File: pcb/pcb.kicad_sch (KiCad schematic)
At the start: 39 parts, among them J3 BAT, U1 xiao-ble

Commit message: rename to Charma
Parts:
- DL1, DL10, DL11, DL12, DL13, DL14, DL15, DL17, DL18, DL19, DL2, DL3, DL4, DL5, DL6, DL7, DL8, DL9: footprint karmalib:Diode_SOD123 -> charmalib:Diode_SOD123
- RSW1: footprint karmalib:SKHLLCA010 -> charmalib:SKHLLCA010
- SWL1, SWL10, SWL11, SWL12, SWL13, SWL14, SWL15, SWL17, SWL18, SWL19, SWL2, SWL3, SWL4, SWL5, SWL6, SWL7, SWL8, SWL9: footprint karmalib:Kailh_Socket_PG1350_Optional -> charmalib:Kailh_Socket_PG1350_Optional
- U1: footprint karmalib:XIAO_nRF52840_SMD_Cutout -> charmalib:XIAO_nRF52840_SMD_Cutout
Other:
- title: Karma Wireless Split Ergonomic Keyboard -> Charma Wireless Split Ergonomic Keyboard
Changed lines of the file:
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@@
 	(paper "User" 200 200)
 	(title_block
-		(title "Karma Wireless Split Ergonomic Keyboard")
+		(title "Charma Wireless Split Ergonomic Keyboard")
 		(date "2023-04-04")
 		(rev "0.32")
@@
 			)
 		)
-		(property "Footprint" "karmalib:Kailh_Socket_PG1350_Optional"
+		(property "Footprint" "charmalib:Kailh_Socket_PG1350_Optional"
 			(at 62.23 99.187 0)
 			(effects
@@
 			)
 		)
-		(property "Footprint" "karmalib:Kailh_Socket_PG1350_Optional"
+		(property "Footprint" "charmalib:Kailh_Socket_PG1350_Optional"
 			(at 72.898 69.215 0)
 			(effects
@@
 			)
 		)
-		(property "Footprint" "karmalib:Diode_SOD123"
+		(property "Footprint" "charmalib:Diode_SOD123"
 			(at 86.106 104.267 90)
 			(effects
@@
 			)
 		)
-		(property "Footprint" "karmalib:Diode_SOD123"
+		(property "Footprint" "charmalib:Diode_SOD123"
 			(at 43.434 74.295 90)
 			(effects
@@
 			)
 		)
-		(property "Footprint" "karmalib:Diode_SOD123"
+		(property "Footprint" "charmalib:Diode_SOD123"
 			(at 75.438 74.295 90)
 			(effects
@@
 			)
 		)
-		(property "Footprint" "karmalib:SKHLLCA010"
+		(property "Footprint" "charmalib:SKHLLCA010"
 			(at 148.0312 131.4704 0)
 			(effects
@@
 			)
 		)
-		(property "Footprint" "karmalib:Kailh_Socket_PG1350_Optional"
+		(property "Footprint" "charmalib:Kailh_Socket_PG1350_Optional"
 			(at 83.566 54.229 0)
 			(effects
@@
 			)
 		)
-		(property "Footprint" "karmalib:Kailh_Socket_PG1350_Optional"
+		(property "Footprint" "charmalib:Kailh_Socket_PG1350_Optional"
 			(at 51.562 69.215 0)
 			(effects
@@
 			)
 		)
-		(property "Footprint" "karmalib:Kailh_Socket_PG1350_Optional"
+		(property "Footprint" "charmalib:Kailh_Socket_PG1350_Optional"
 			(at 40.894 84.201 0)
 			(effects
@@
 			)
 		)
-		(property "Footprint" "karmalib:Diode_SOD123"
+		(property "Footprint" "charmalib:Diode_SOD123"
 			(at 86.106 89.281 90)
 			(effects
@@
 			)
 		)
-		(property "Footprint" "karmalib:Kailh_Socket_PG1350_Optional"
+		(property "Footprint" "charmalib:Kailh_Socket_PG1350_Optional"
 			(at 83.566 69.215 0)
 			(effects
@@
 			)
 		)
-		(property "Footprint" "karmalib:Kailh_Socket_PG1350_Optional"
+		(property "Footprint" "charmalib:Kailh_Socket_PG1350_Optional"
 			(at 62.23 54.229 0)
 			(effects
@@
 			)
 		)
-		(property "Footprint" "karmalib:Kailh_Socket_PG1350_Optional"
+		(property "Footprint" "charmalib:Kailh_Socket_PG1350_Optional"
 			(at 72.898 84.201 0)
 			(effects
@@
 			)
 		)
-		(property "Footprint" "karmalib:Diode_SOD123"
+		(property "Footprint" "charmalib:Diode_SOD123"
 			(at 43.434 89.281 90)
 			(effects
@@
 			)
 		)
-		(property "Footprint" "karmalib:Kailh_Socket_PG1350_Optional"
+		(property "Footprint" "charmalib:Kailh_Socket_PG1350_Optional"
 			(at 62.23 69.215 0)
 			(effects
@@
 			)
 		)
-		(property "Footprint" "karmalib:Kailh_Socket_PG1350_Optional"
+		(property "Footprint" "charmalib:Kailh_Socket_PG1350_Optional"
 			(at 62.23 84.201 0)
 			(effects
@@
 			)
 		)
-		(property "Footprint" "karmalib:Diode_SOD123"
+		(property "Footprint" "charmalib:Diode_SOD123"
 			(at 64.77 104.267 90)
 			(effects
@@
 			)
 		)
-		(property "Footprint" "karmalib:Diode_SOD123"
+		(property "Footprint" "charmalib:Diode_SOD123"
 			(at 64.77 74.295 90)
 			(effects
@@
 			)
 		)
-		(property "Footprint" "karmalib:Diode_SOD123"
+		(property "Footprint" "charmalib:Diode_SOD123"
 			(at 75.438 59.309 90)
 			(effects
@@
 			)
 		)
-		(property "Footprint" "karmalib:Kailh_Socket_PG1350_Optional"
+		(property "Footprint" "charmalib:Kailh_Socket_PG1350_Optional"
 			(at 83.566 99.187 0)
 			(effects
@@
 			)
 		)
-		(property "Footprint" "karmalib:Kailh_Socket_PG1350_Optional"
+		(property "Footprint" "charmalib:Kailh_Socket_PG1350_Optional"
 			(at 40.894 69.215 0)
 			(effects
@@
 			)
 		)
-		(property "Footprint" "karmalib:Kailh_Socket_PG1350_Optional"
+		(property "Footprint" "charmalib:Kailh_Socket_PG1350_Optional"
 			(at 51.562 84.201 0)
 			(effects
@@
 			)
 		)
-		(property "Footprint" "karmalib:Kailh_Socket_PG1350_Optional"
+		(property "Footprint" "charmalib:Kailh_Socket_PG1350_Optional"
 			(at 51.562 54.229 0)
 			(effects
@@
 			)
 		)
-		(property "Footprint" "karmalib:Kailh_Socket_PG1350_Optional"
+		(property "Footprint" "charmalib:Kailh_Socket_PG1350_Optional"
 			(at 40.894 54.229 0)
 			(effects
@@
 			)
 		)
-		(property "Footprint" "karmalib:Kailh_Socket_PG1350_Optional"
+		(property "Footprint" "charmalib:Kailh_Socket_PG1350_Optional"
 			(at 72.898 54.229 0)
 			(effects
@@
 			)
 		)
-		(property "Footprint" "karmalib:Diode_SOD123"
+		(property "Footprint" "charmalib:Diode_SOD123"
 			(at 54.102 59.309 90)
 			(effects
@@
 			)
 		)
-		(property "Footprint" "karmalib:Diode_SOD123"
+		(property "Footprint" "charmalib:Diode_SOD123"
 			(at 64.77 59.309 90)
 			(effects
@@
 			)
 		)
-		(property "Footprint" "karmalib:XIAO_nRF52840_SMD_Cutout"
+		(property "Footprint" "charmalib:XIAO_nRF52840_SMD_Cutout"
 			(at 134.6708 68.7578 0)
 			(effects
@@
 			)
 		)
-		(property "Footprint" "karmalib:Diode_SOD123"
+		(property "Footprint" "charmalib:Diode_SOD123"
 			(at 43.434 59.309 90)
 			(effects
@@
 			)
 		)
-		(property "Footprint" "karmalib:Diode_SOD123"
+		(property "Footprint" "charmalib:Diode_SOD123"
 			(at 54.102 89.281 90)
 			(effects
@@
 			)
 		)
-		(property "Footprint" "karmalib:Kailh_Socket_PG1350_Optional"
+		(property "Footprint" "charmalib:Kailh_Socket_PG1350_Optional"
 			(at 72.898 99.187 0)
 			(effects
@@
 			)
 		)
-		(property "Footprint" "karmalib:Diode_SOD123"
+		(property "Footprint" "charmalib:Diode_SOD123"
 			(at 75.438 104.267 90)
 			(effects
@@
 			)
 		)
-		(property "Footprint" "karmalib:Diode_SOD123"
+		(property "Footprint" "charmalib:Diode_SOD123"
 			(at 54.102 74.295 90)
 			(effects
@@
 			)
 		)
-		(property "Footprint" "karmalib:Diode_SOD123"
+		(property "Footprint" "charmalib:Diode_SOD123"
 			(at 75.438 89.281 90)
 			(effects
@@
 			)
 		)
-		(property "Footprint" "karmalib:Diode_SOD123"
+		(property "Footprint" "charmalib:Diode_SOD123"
 			(at 86.106 74.295 90)
 			(effects
@@
 			)
 		)
-		(property "Footprint" "karmalib:Diode_SOD123"
+		(property "Footprint" "charmalib:Diode_SOD123"
 			(at 86.106 59.309 90)
 			(effects
@@
 			)
 		)
-		(property "Footprint" "karmalib:Kailh_Socket_PG1350_Optional"
+		(property "Footprint" "charmalib:Kailh_Socket_PG1350_Optional"
 			(at 83.566 84.201 0)
 			(effects
@@
 			)
 		)
-		(property "Footprint" "karmalib:Diode_SOD123"
+		(property "Footprint" "charmalib:Diode_SOD123"
 			(at 64.77 89.281 90)
 			(effects

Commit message: Parameterise
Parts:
- added DR19, DR20, DR21, DR22, DR23, DR24, DR25, DR26, DR27, DR28, DR29, DR30, DR31, DR32, DR33, DR34, DR35, DR36: D_Small, charmalib:Diode_SOD123, symbol Device:D_Small
- added J2: BAT, Connector_PinHeader_2.54mm:PinHeader_1x02_P2.54mm_Vertical, symbol Connector_Generic:Conn_01x02
- added RSW2: SW_Push, Button_Switch_SMD:SW_Push_1P1T-MP_NO_Horizontal_Alps_SKRTLAE010, symbol Switch:SW_Push
- added SWR1, SWR19, SWR2, SWR20, SWR21, SWR22, SWR23, SWR24, SWR25, SWR26, SWR27, SWR28, SWR29, SWR3, SWR4, SWR5, SWR6, SWR7: SW_Push_45deg, charmalib:Kailh_Socket_PG1350_Optional, symbol Switch:SW_Push_45deg
- added U2: xiao-ble, charmalib:XIAO_nRF52840_SMD_Cutout, symbol mcu:xiao-ble
- RSW1: footprint charmalib:SKHLLCA010 -> Button_Switch_SMD:SW_Push_1P1T-MP_NO_Horizontal_Alps_SKRTLAE010
- renumbered DL17 to DL16, DL18 to DL17, DL19 to DL18, J3 to J1, SWL17 to SWL16, SWL18 to SWL17, SWL19 to SWL18
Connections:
- new net: DR21.2 (A), SWR3.2
- new net: DR30.2 (A), SWR23.2
- new net: DR25.2 (A), SWR7.2
- new net: DR19.2 (A), SWR1.2
- new net: DR35.2 (A), SWR28.2
- new net: DR24.2 (A), SWR6.2
- new net: DR36.2 (A), SWR29.2
- new net: DR20.2 (A), SWR2.2
- new net: DR22.2 (A), SWR4.2
- new net: DR27.2 (A), SWR20.2
- new net: DR31.2 (A), SWR24.2
- new net: DR33.2 (A), SWR26.2
- new net: DR28.2 (A), SWR21.2
- new net: DR23.2 (A), SWR5.2
- new net: DR26.2 (A), SWR19.2
- new net: DR29.2 (A), SWR22.2
- new net: DR34.2 (A), SWR27.2
- new net: DR32.2 (A), SWR25.2
- new net COL0_R: SWR1.1, SWR22.1, SWR6.1, U2.5 (A8_SDA/0.04_H)
- new net COL1_R: SWR2.1, SWR23.1, SWR7.1, U2.6 (A9_SCL/0.05_H)
- new net COL2_R: SWR19.1, SWR24.1, SWR27.1, SWR3.1, U2.11 (A6_MOSI/1.15)
- new net COL3_R: SWR20.1, SWR25.1, SWR28.1, SWR4.1, U2.10 (A5_MISO/1.14)
- new net COL4_R: SWR21.1, SWR26.1, SWR29.1, SWR5.1, U2.9 (A7_SCK/1.13)
- new net GND_R: J2.1 (Pin_1), RSW2.2, U2.13 (GND), U2.18 (GND), U2.20 (GND)
- new net RESET_R: RSW2.1, U2.17 (RESET)
- new net ROW0_R: DR19.1 (K), DR20.1 (K), DR21.1 (K), DR22.1 (K), DR23.1 (K), U2.4 (A11/0.29)
- new net ROW1_R: DR24.1 (K), DR25.1 (K), DR26.1 (K), DR27.1 (K), DR28.1 (K), U2.3 (A10/0.28)
- new net ROW2_R: DR29.1 (K), DR30.1 (K), DR31.1 (K), DR32.1 (K), DR33.1 (K), U2.2 (A4/0.03_H)
- new net ROW3_R: DR34.1 (K), DR35.1 (K), DR36.1 (K), U2.1 (A2/0.02_H)
- new net VBAT_R: J2.2 (Pin_2), U2.19 (BAT)
- no-connect marks 8 -> 16

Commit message: Update refs
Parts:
- renumbered J1 to BATL1, J2 to BATR1, DR19 to DR1, DR28 to DR10, DR29 to DR11, DR30 to DR12, DR31 to DR13, DR32 to DR14, DR33 to DR15, DR34 to DR16, DR35 to DR17, DR36 to DR18, DR20 to DR2, DR21 to DR3, DR22 to DR4, DR23 to DR5, DR24 to DR6, DR25 to DR7, DR26 to DR8, DR27 to DR9, U1 to MCUL1, U2 to MCUR2, RSW1 to RSWL1, RSW2 to RSWR1, SWR21 to SWR10, SWR22 to SWR11, SWR23 to SWR12, SWR24 to SWR13, SWR25 to SWR14, SWR26 to SWR15, SWR27 to SWR16, SWR28 to SWR17, SWR29 to SWR18, SWR19 to SWR8, SWR20 to SWR9

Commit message: Use SKQB for reset
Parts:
- RSWL1, RSWR1: footprint Button_Switch_SMD:SW_Push_1P1T-MP_NO_Horizontal_Alps_SKRTLAE010 -> Button_Switch_SMD:SW_SPST_SKQG_WithStem
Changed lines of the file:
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@@
 			)
 		)
-		(property "Footprint" "Button_Switch_SMD:SW_Push_1P1T-MP_NO_Horizontal_Alps_SKRTLAE010"
+		(property "Footprint" "Button_Switch_SMD:SW_SPST_SKQG_WithStem"
 			(at 344.3732 131.8514 0)
 			(effects
@@
 			)
 		)
-		(property "Footprint" "Button_Switch_SMD:SW_Push_1P1T-MP_NO_Horizontal_Alps_SKRTLAE010"
+		(property "Footprint" "Button_Switch_SMD:SW_SPST_SKQG_WithStem"
 			(at 148.0312 131.4704 0)
 			(effects

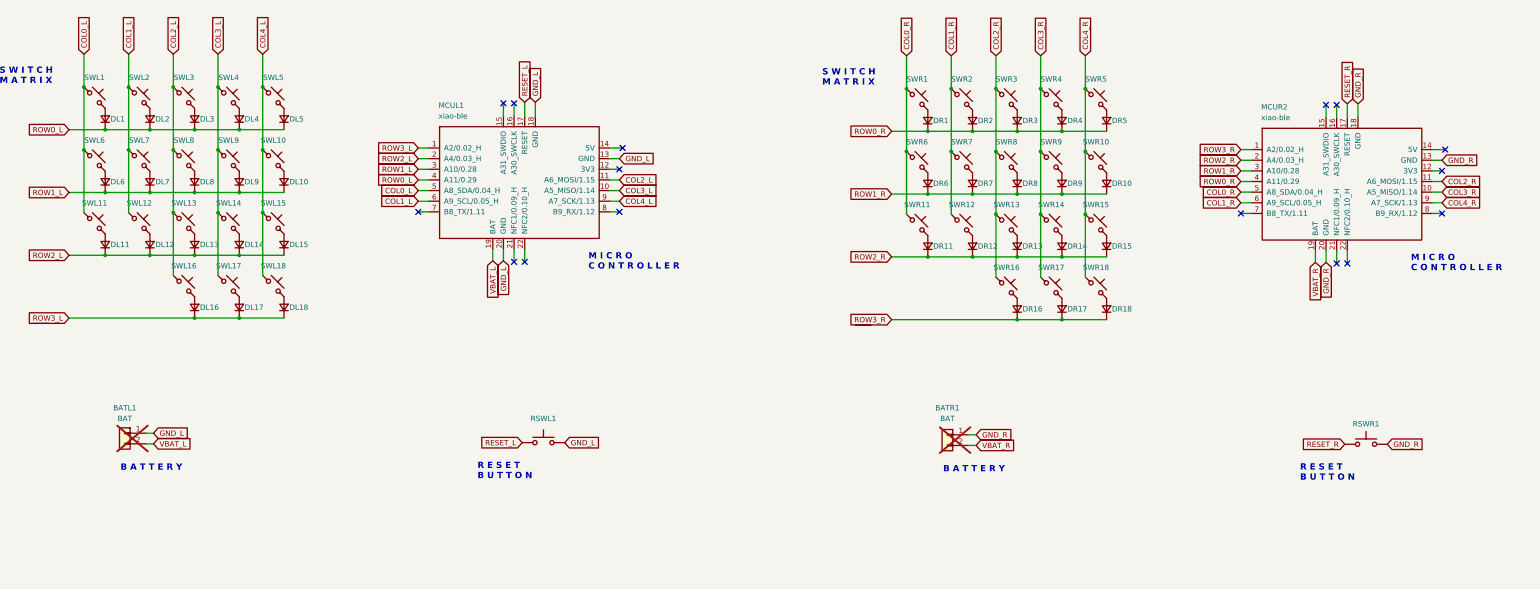
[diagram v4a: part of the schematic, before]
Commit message: Use socketed Xiao
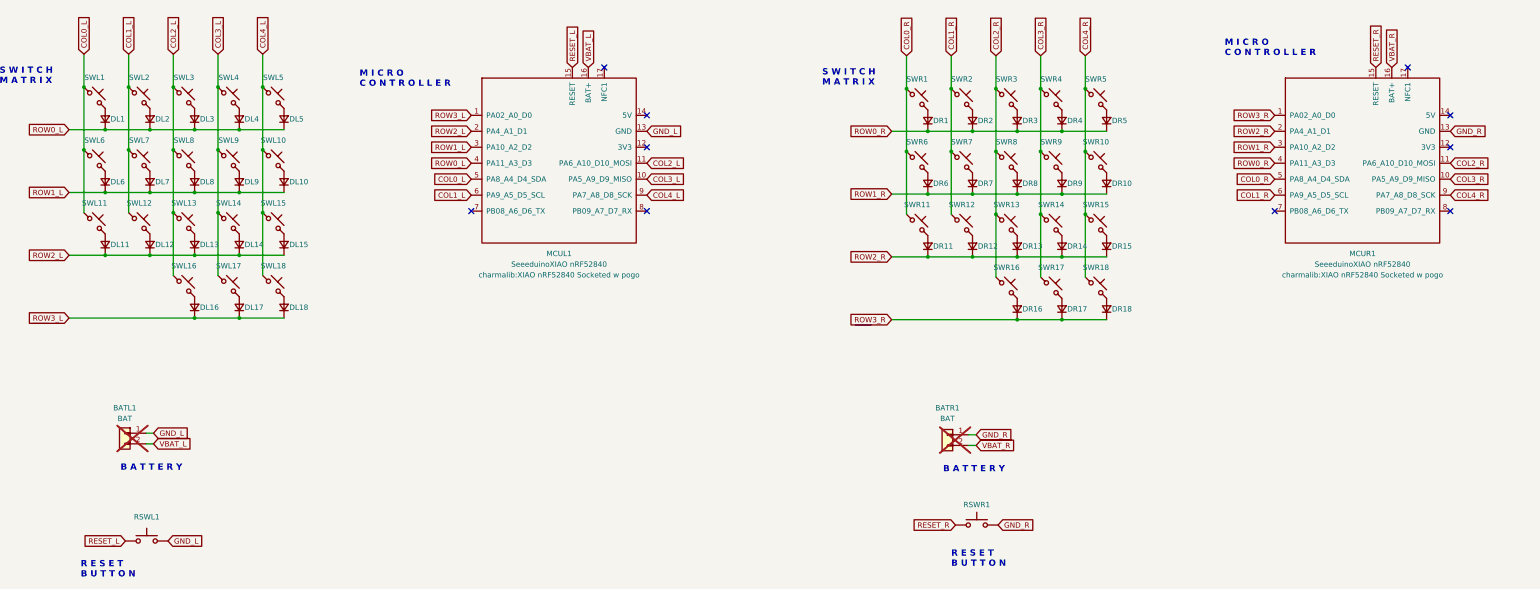
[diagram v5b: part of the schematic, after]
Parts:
- removed MCUL1, MCUR2: xiao-ble, charmalib:XIAO_nRF52840_SMD_Cutout, symbol mcu:xiao-ble
- added MCUL1, MCUR1: SeeeduinoXIAO nRF52840, charmalib:XIAO nRF52840 Socketed w pogo, symbol Xiao:Xiao nRF52840
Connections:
- net COL0_L: now also MCUL1.5 (PA8_A4_D4_SDA)
- net COL0_R: now also MCUR1.5 (PA8_A4_D4_SDA)
- net COL1_L: now also MCUL1.6 (PA9_A5_D5_SCL)
- net COL1_R: now also MCUR1.6 (PA9_A5_D5_SCL)
- net COL2_L: now also MCUL1.11 (PA6_A10_D10_MOSI)
- net COL2_R: now also MCUR1.11 (PA6_A10_D10_MOSI)
- net COL3_L: now also MCUL1.10 (PA5_A9_D9_MISO)
- net COL3_R: now also MCUR1.10 (PA5_A9_D9_MISO)
- net COL4_L: now also MCUL1.9 (PA7_A8_D8_SCK)
- net COL4_R: now also MCUR1.9 (PA7_A8_D8_SCK)
- net GND_L: now also MCUL1.13 (GND)
- net GND_R: now also MCUR1.13 (GND)
- net RESET_L: now also MCUL1.15 (RESET)
- net RESET_R: now also MCUR1.15 (RESET)
- net ROW0_L: now also MCUL1.4 (PA11_A3_D3)
- net ROW0_R: now also MCUR1.4 (PA11_A3_D3)
- net ROW1_L: now also MCUL1.3 (PA10_A2_D2)
- net ROW1_R: now also MCUR1.3 (PA10_A2_D2)
- net ROW2_L: now also MCUL1.2 (PA4_A1_D1)
- net ROW2_R: now also MCUR1.2 (PA4_A1_D1)
- net ROW3_L: now also MCUL1.1 (PA02_A0_D0)
- net ROW3_R: now also MCUR1.1 (PA02_A0_D0)
- net VBAT_L: now also MCUL1.16 (BAT+)
- net VBAT_R: now also MCUR1.16 (BAT+)
- no-connect marks 16 -> 10
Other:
- moved on the sheet: RSWL1, RSWR1

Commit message: Logo
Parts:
- added PSWL1, PSWR1: SW_SPDT, Button_Switch_SMD:SW_SPDT_PCM12, symbol Switch:SW_SPDT
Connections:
- net COL0_R: now also SWR18.1
- net COL1_R: now also SWR17.1
- net COL3_R: no longer SWR17.1
- net COL4_R: no longer SWR18.1
- net VBAT_L: now also PSWL1.2 (B); no longer MCUL1.16 (BAT+)
- net VBAT_R: now also PSWR1.2 (B); no longer MCUR1.16 (BAT+)
- new net MCU_BAT+_L: MCUL1.16 (BAT+), PSWL1.3 (C)
- new net MCU_BAT+_R: MCUR1.16 (BAT+), PSWR1.3 (C)
- no-connect marks 10 -> 12
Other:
- moved on the sheet: DR10, DR11, DR12, DR13, DR14, DR15, DR16, DR17, DR18, DR2, DR3, DR4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

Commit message: Route and silkscreen
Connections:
- net COL0_R: now also MCUR1.7 (PB08_A6_D6_TX); no longer MCUR1.5 (PA8_A4_D4_SDA)
- net COL2_R: now also MCUR1.5 (PA8_A4_D4_SDA); no longer MCUR1.11 (PA6_A10_D10_MOSI)
- net COL3_R: now also MCUR1.4 (PA11_A3_D3); no longer MCUR1.10 (PA5_A9_D9_MISO)
- net COL4_R: now also MCUR1.3 (PA10_A2_D2); no longer MCUR1.9 (PA7_A8_D8_SCK)
- net GND_L: now also RSWL1.1; no longer RSWL1.2
- net RESET_L: now also RSWL1.2; no longer RSWL1.1
- net ROW0_R: now also MCUR1.8 (PB09_A7_D7_RX); no longer MCUR1.4 (PA11_A3_D3)
- net ROW1_R: now also MCUR1.9 (PA7_A8_D8_SCK); no longer MCUR1.3 (PA10_A2_D2)
- net ROW2_R: now also MCUR1.10 (PA5_A9_D9_MISO); no longer MCUR1.2 (PA4_A1_D1)
- net ROW3_R: now also MCUR1.11 (PA6_A10_D10_MOSI); no longer MCUR1.1 (PA02_A0_D0)
- no-connect marks 12 -> 13
